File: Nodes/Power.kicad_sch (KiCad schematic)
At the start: 19 parts, among them IC6 TPS22995HQDDCRQ1, T23 Conn_01x01, T3 Conn_01x01, T4 Conn_01x01, T5 Conn_01x01, T6 Conn_01x01, T7 Conn_01x01, T8 Conn_01x01

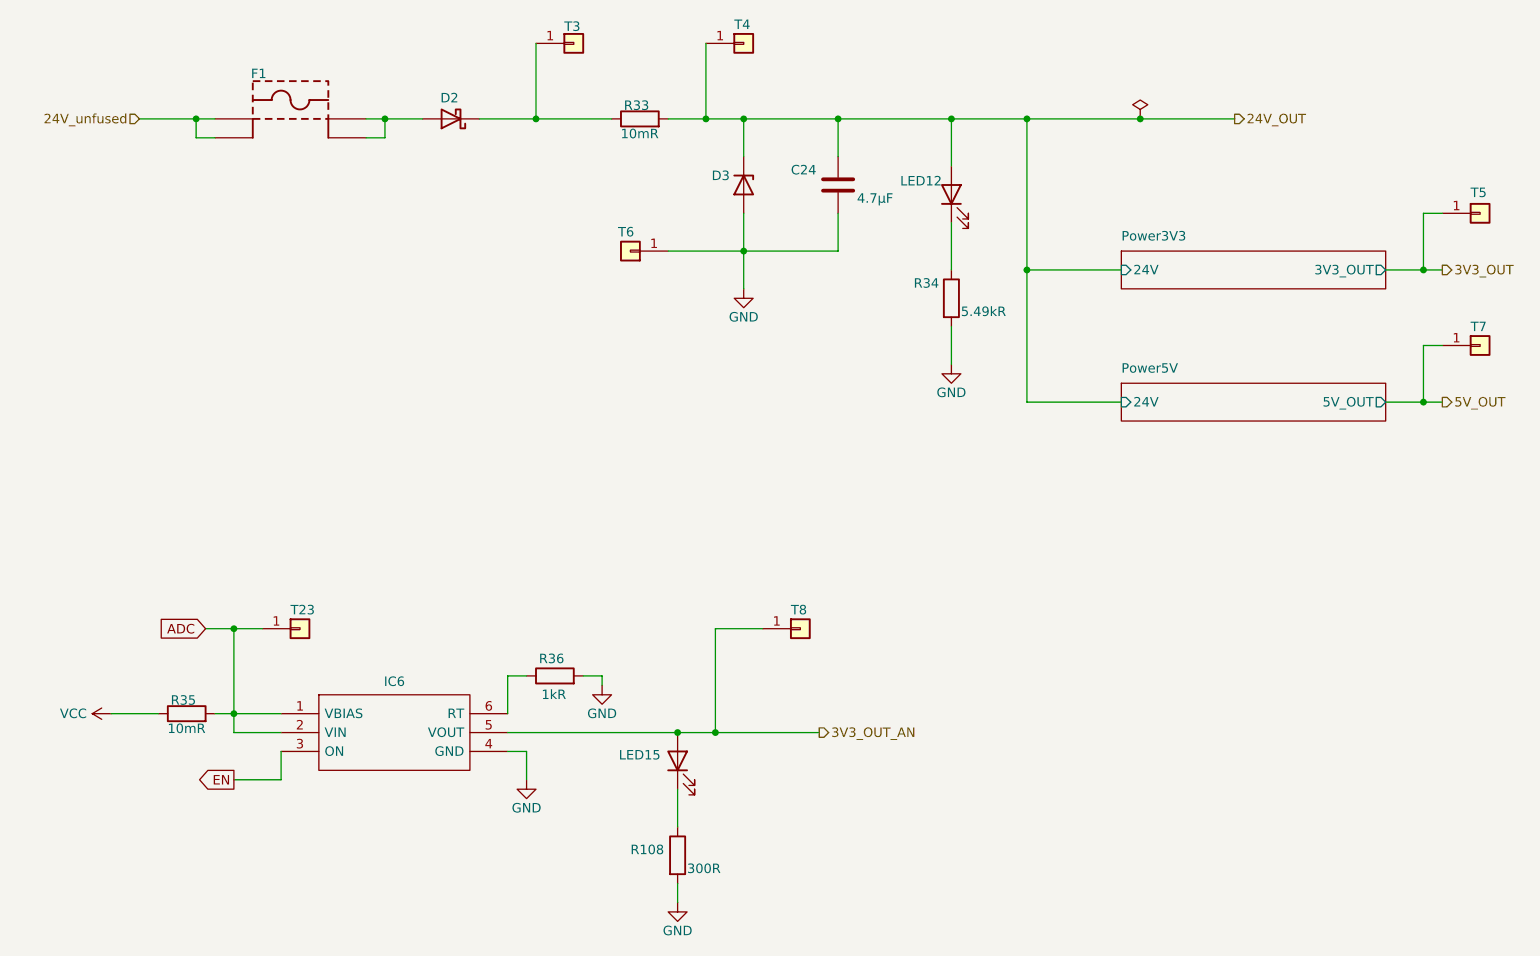
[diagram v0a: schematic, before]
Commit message: Nodes v2.1.2 Improved
- Improved schematic design
- Added two 4.7 uF caps according to the datasheets of the microchips
- Other small changes
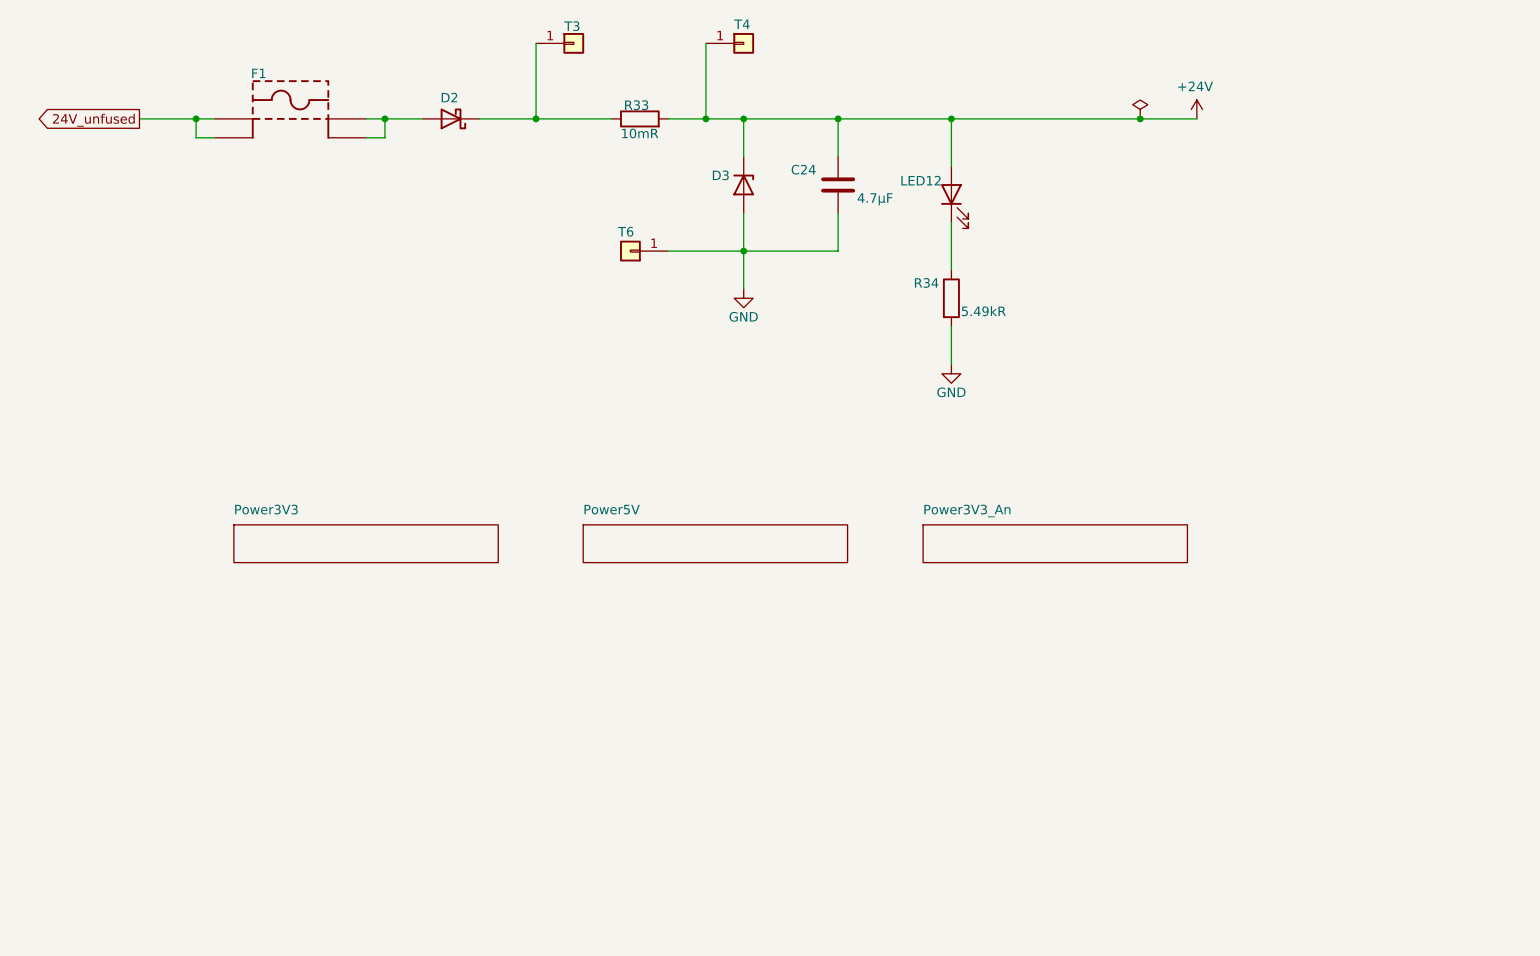
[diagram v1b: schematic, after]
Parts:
- removed IC6: TPS22995HQDDCRQ1, Button_Switch_SMD:SOT95P280X110-6N, symbol Power_Switch:TPS22995HQDDCRQ1
- removed LED15: 150080BS75000, LED_SMD:LED_0805_2012Metric_Pad1.15x1.40mm_HandSolder, symbol Device:LED
- removed R108: 300R, Resistor_SMD:R_0805_2012Metric_Pad1.20x1.40mm_HandSolder, symbol Device:R
- removed R35: 10mR, Resistor_SMD:R_0805_2012Metric_Pad1.20x1.40mm_HandSolder, symbol Device:R
- removed R36: 1kR, Resistor_SMD:R_0805_2012Metric_Pad1.20x1.40mm_HandSolder, symbol Device:R
- removed T23, T5, T7, T8: Conn_01x01, TestPoint:TestPoint_THTPad_D1.5mm_Drill0.7mm, symbol Connector_Generic:Conn_01x01
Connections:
- net 24V_OUT renamed +24V
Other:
- added sheet Power3V3_An (Power3V3_An.kicad_sch)
- sheet Power3V3 ports: added none; removed 24V, 3V3_OUT
- sheet Power5V ports: added none; removed 24V, 5V_OUT

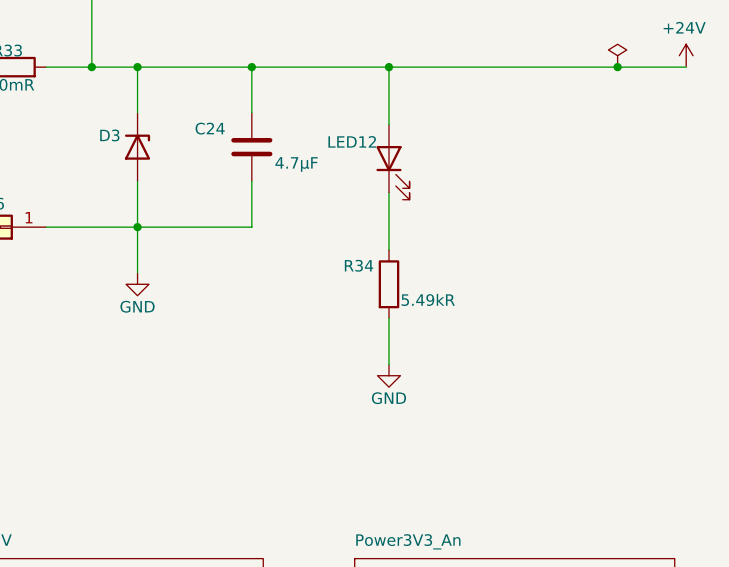
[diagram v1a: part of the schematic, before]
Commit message: Nodes v2.2
- This version not compatible with BOB v.2.1.2 and older!
- Completely new layout design
- New power supply system with new voltage regulators
- New microchip STM32G431RBTx for the Analog Node
- New connection system (instead of 18 pin headers now 8 pin and pins were grouped by functions)
- Reduced size of the board by 5%
- Removed power switch for the Analog Node (because this functionality is now provided by a separate voltage regulator. for a more stable voltage)
- Removable ground from the holes added
- Layer numbers added
- Small improvements of the components information were made
- New oscillator for the Nodes
- Removed CAN1, so now only one CAN connection due to the capabilities of the new microchip
- Other small changes and fixes on the schematic and design
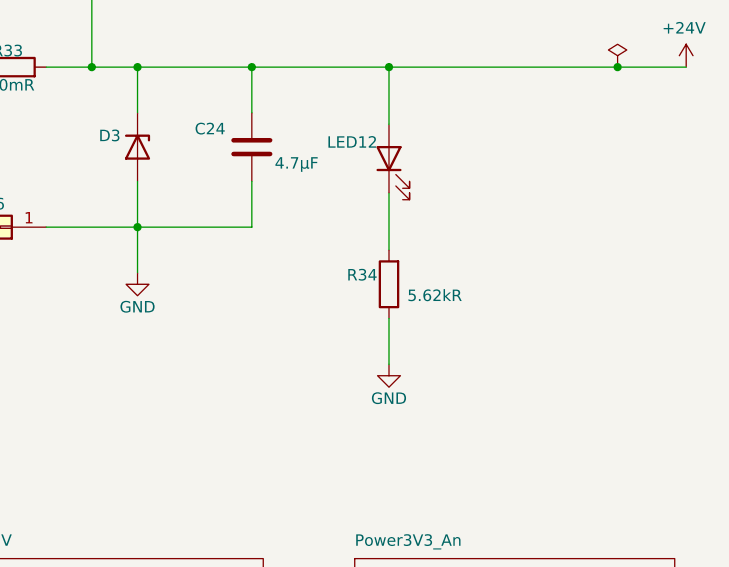
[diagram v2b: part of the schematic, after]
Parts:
- D2: value BYS10-25-E3 -> SX33L_R1_00001; ADDITIONAL FEATURE HIGH RELIABILITY -> (none); DIODE ELEMENT MATERIAL SILICON -> (none); DIODE TYPE RECTIFIER -> (none); FORWARD VOLTAGE 1.1V -> (none); JESD-30 CODE R-PDSO-C2 -> (none); JESD-609 CODE e3 -> (none); MAX OPERATING TEMPERATURE 150°C -> (none); MAX OUTPUT CURRENT 1A -> (none); MIN OPERATING TEMPERATURE -65°C -> (none); MOISTURE SENSITIVITY LEVEL 1 -> (none); NON-REP PK FORWARD CURRENT-MAX 30A -> (none); NUMBER OF ELEMENTS 1 -> (none); PACKAGE BODY MATERIAL Plastic -> (none); PACKAGE SHAPE Rectangular -> (none); PACKAGE STYLE SMALL OUTLINEMeter -> (none); PEAK REFLOW TEMPERATURE (CEL) 260°C -> (none); PINS 2 -> (none); QUALIFICATION STATUS Not Qualified -> (none); REACH SVHC COMPLIANT No -> (none); REP PK REVERSE VOLTAGE-MAX 1kV -> (none); REVERSE RECOVERY TIME-MAX 3us -> (none); ROHS COMPLIANT Yes -> (none); SURFACE MOUNT Yes -> (none); TERMINAL FINISH Tin -> (none); TERMINAL FORM C BEND -> (none); TERMINAL POSITION DUAL -> (none); TIME @ PEAK REFLOW TEMPERATURE-MAX (S) 40s -> (none)
- R34: value 5.49kR -> 5.62kR; ALTIUM_VALUE 5.49kR -> (none); AUTOMOTIVE Yes -> (none); AUTOMOTIVE GRADE Grade 0 -> (none); CATEGORY Res -> (none); COMPONENTLINK2DESCRIPTION Datasheet -> (none); COMPONENTLINK2URL http://www.yageo.com/documents/recent/PYu-AC_51_RoHS_L_6.pdf -> (none); COMPOSITION Thick Film -> (none); DEVICE CLASS L1 Passive Components -> (none); DEVICE CLASS L2 Resistors -> (none); DEVICE CLASS L3 Chip SMD Resistors -> (none); DIGIKEY DESCRIPTION Res SMD 5.49K Ohm 1% 1/8W 0805 -> (none); FOOTPRINT URL http://www.yageo.com/exep/pages/download/literatures/PYu-R_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 -> (none); HEIGHT 0.6mm -> (none); IPC LAND PATTERN NAME RESC200125X50 -> (none); LEAD FREE Yes -> (none); MANUFACTURER Yageo -> (none); MANUFACTURER PART NUMBER AC0805FR-075K49L -> (none); OCTOPART https://octopart.com/ac0805fr-075k49l-yageo-71367778 -> (none); PACKAGE AC0805 -> (none); POWER RATING 1/8W -> (none); RESISTANCE 5.49KΩ -> (none); ROHS TRUE -> (none); SERIES AC -> (none); TEMPERATURE -55°C to +155°C -> (none); TEMPERATURE RANGE HIGH +155°C -> (none); TEMPERATURE RANGE LOW -55°C -> (none); TOLERANCE 0.01 -> (none); VOLTAGE RATING 150V -> (none)
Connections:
- net GND: now also R34.1; no longer R34.2
- net at LED12.1 (K): now also R34.2; no longer R34.1
